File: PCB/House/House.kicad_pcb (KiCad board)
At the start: 2 copper layers, 60 x 35.5 mm, 21 parts, among them J1 Conn_01x05, U1 HT16K33-28SOP

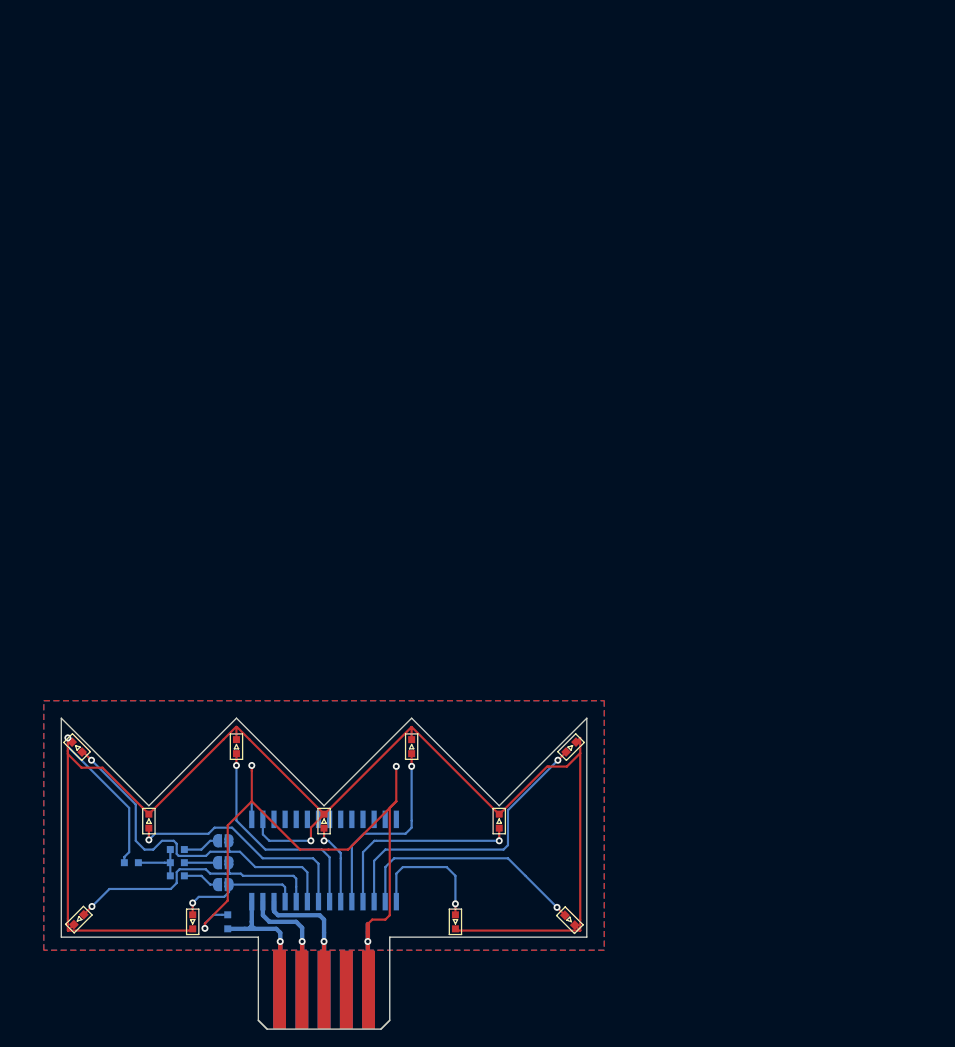
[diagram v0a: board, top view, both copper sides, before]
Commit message: [update] HouseのLED仮位置決め完了
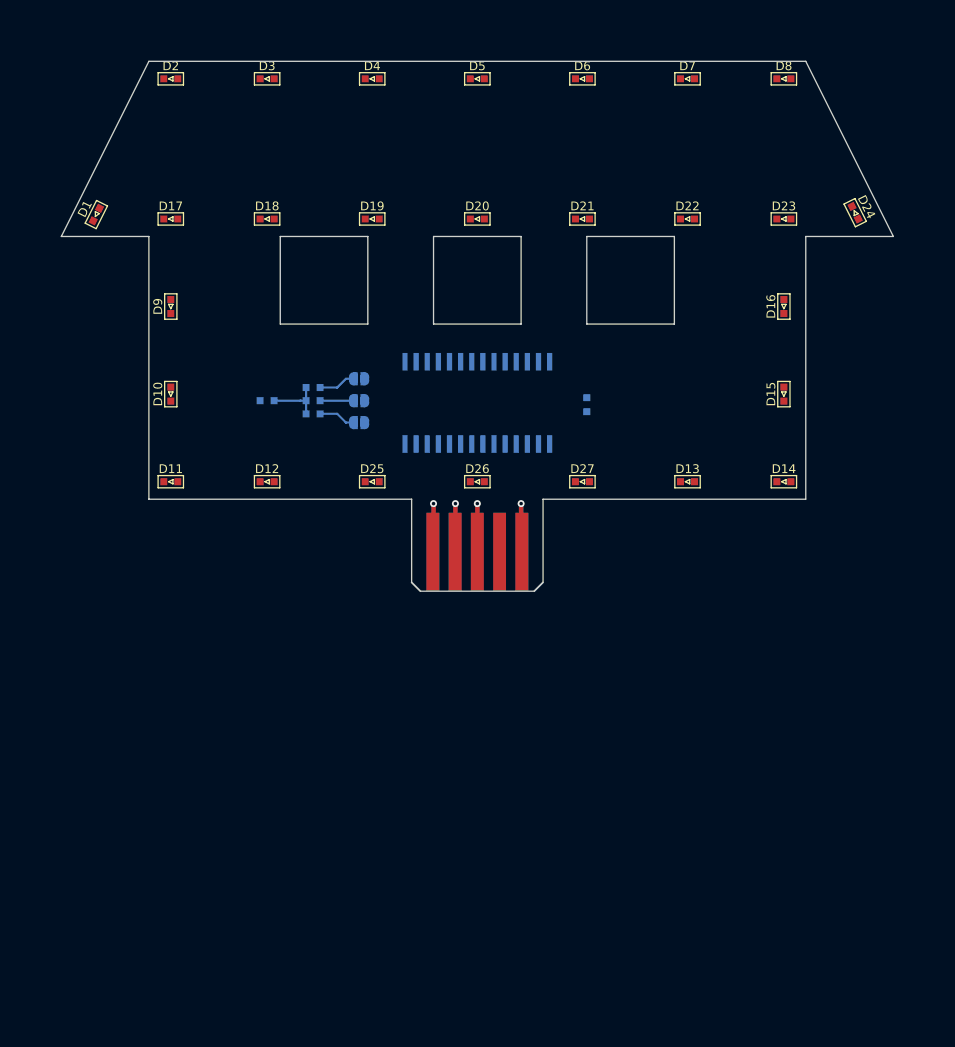
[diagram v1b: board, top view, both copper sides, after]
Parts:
- added D13: LED, extsui:LED_1608_HandSolderingCustom, F.Cu at (171.5, 98.0)
- added D14: LED, extsui:LED_1608_HandSolderingCustom, F.Cu at (182.5, 98.0)
- added D15: LED, extsui:LED_1608_HandSolderingCustom, F.Cu at (182.5, 88.0)
- added D16: LED, extsui:LED_1608_HandSolderingCustom, F.Cu at (182.5, 78.0)
- added D17: LED, extsui:LED_1608_HandSolderingCustom, F.Cu at (112.5, 68.0)
- added D18: LED, extsui:LED_1608_HandSolderingCustom, F.Cu at (123.5, 68.0)
- added D19: LED, extsui:LED_1608_HandSolderingCustom, F.Cu at (135.5, 68.0)
- added D20: LED, extsui:LED_1608_HandSolderingCustom, F.Cu at (147.5, 68.0)
- added D21: LED, extsui:LED_1608_HandSolderingCustom, F.Cu at (159.5, 68.0)
- added D22: LED, extsui:LED_1608_HandSolderingCustom, F.Cu at (171.5, 68.0)
- added D23: LED, extsui:LED_1608_HandSolderingCustom, F.Cu at (182.5, 68.0)
- added D24: LED, extsui:LED_1608_HandSolderingCustom, F.Cu at (190.6, 67.3)
- added D25: LED, extsui:LED_1608_HandSolderingCustom, F.Cu at (135.5, 98.0)
- added D26: LED, extsui:LED_1608_HandSolderingCustom, F.Cu at (147.5, 98.0)
- added D27: LED, extsui:LED_1608_HandSolderingCustom, F.Cu at (159.5, 98.0)
- added D28: D, extsui:LED_1608_HandSolderingCustom, B.Cu at (123.5, 88.8)
- D1, D10, D11, D2, D3, D4, D5, D6, D7, D8, D9: value GLED -> LED
- D12: value D -> LED; moved to F.Cu
- moved D2 96.6 mm to (112.5, 52.0), turned to 0 degrees
- moved D8 90.8 mm to (182.5, 52.0), turned to 0 degrees
- moved D6 89.7 mm to (159.5, 52.0), turned to 0 degrees
- moved D4 88.5 mm to (135.5, 52.0), turned to 0 degrees
- moved D7 82.5 mm to (171.5, 52.0), turned to 0 degrees
- moved D1 81.5 mm to (104.0, 67.5), turned to 63.4 degrees
- moved D5 81.1 mm to (147.5, 52.0), turned to 0 degrees
- moved D3 79.3 mm to (123.5, 52.0), turned to 0 degrees
- moved D10 75.4 mm to (112.5, 88.0), turned to 90 degrees
- moved C1 71.9 mm to (160.0, 89.2), turned to 270 degrees
- moved D9 68.0 mm to (112.5, 78.0), turned to 90 degrees
- moved D11 59.8 mm to (112.5, 98.0), turned to 0 degrees
- moved U1 55.1 mm to (147.5, 89.0)
- moved JP1 55.0 mm to (134.0, 91.2)
- moved JP2 55.0 mm to (134.0, 88.8)
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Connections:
- D12 pad 1: Net-(D12-Pad1) -> Net-(D1-Pad1)
- D12 pad 2: Net-(D1-Pad1) -> Net-(D12-Pad2)
- R1 pad 2: Net-(D12-Pad1) -> Net-(D28-Pad1)
- R2 pad 2: Net-(D12-Pad1) -> Net-(D28-Pad1)
- R3 pad 2: Net-(D12-Pad1) -> Net-(D28-Pad1)
- U1 pad 14: Net-(U1-Pad14) -> Net-(D12-Pad2)
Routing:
- net Net-(D1-Pad1): track 188.7 -> 0.00 mm, vias 2 -> 0
- net GND: track 82.9 -> 11.1 mm, vias 4 -> 1
- net Net-(D19-Pad2): track 40.3 -> 0.00 mm, vias 1 -> 0
- net Net-(D25-Pad2): track 34.1 -> 0.00 mm, vias 1 -> 0
- net Net-(D18-Pad2): track 31.5 -> 0.00 mm, vias 1 -> 0
- net Net-(D10-Pad2): track 27.6 -> 0.00 mm, vias 1 -> 0
- net Net-(D20-Pad2): track 27.3 -> 0.00 mm, vias 1 -> 0
- net Net-(D21-Pad2): track 25.1 -> 0.00 mm, vias 1 -> 0
- net Net-(D24-Pad2): track 23.2 -> 0.00 mm, vias 1 -> 0
- net Net-(D23-Pad2): track 22.5 -> 0.00 mm, vias 1 -> 0
- net Net-(D11-Pad2): track 15.1 -> 0.00 mm, vias 1 -> 0
- net Net-(D1-Pad2): track 15.0 -> 0.00 mm, vias 1 -> 0
- net +5V: track 21.9 -> 11.1 mm
- net SCL: track 20.7 -> 11.0 mm
- net Net-(D22-Pad2): track 9.48 -> 0.00 mm, vias 1 -> 0
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- removed copper zone on B.Cu, net GND
- removed copper zone on F.Cu, net GND
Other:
- board size 60 x 35.5 mm -> 95 x 60.5 mm
- board text added: "@ext_sui 2020.01"
- board text added: "House Growing v1.0"
- board text removed: "@ext_sui 2019.11"
- board text removed: "Grass Growing v2.1"

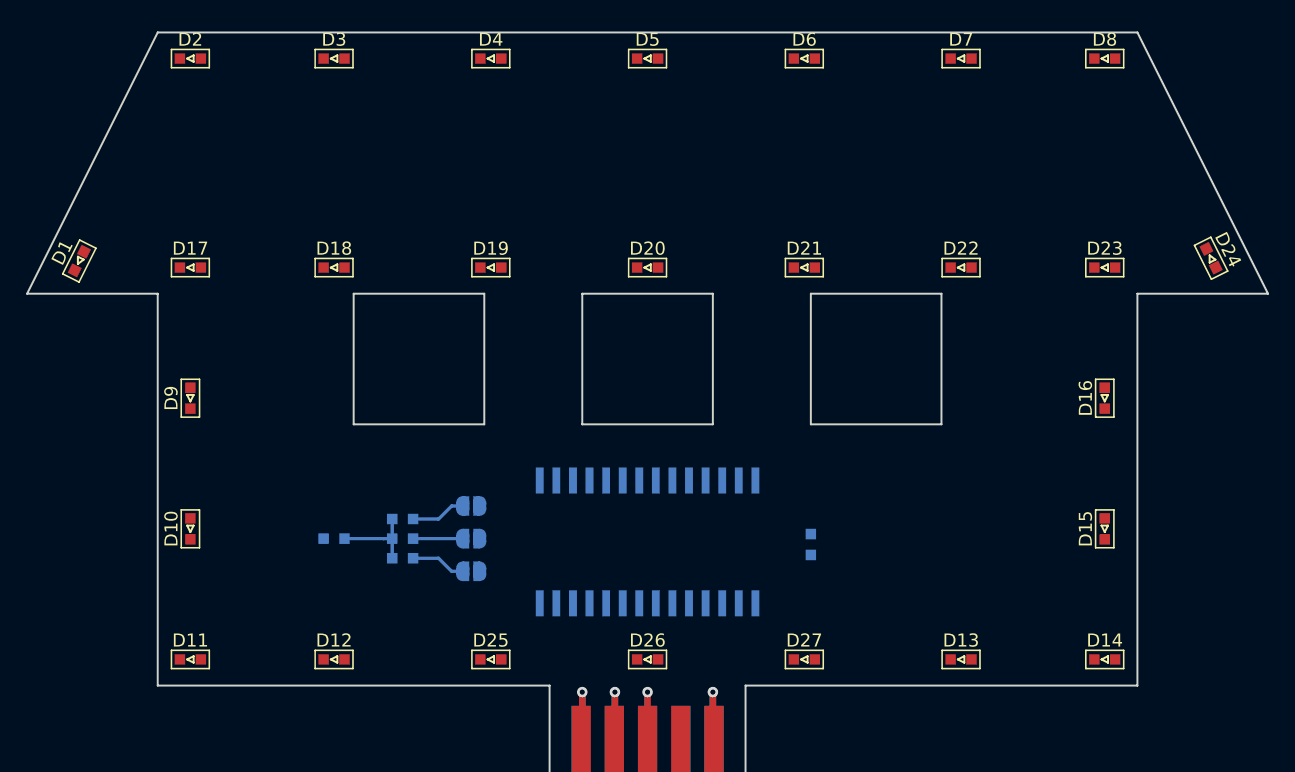
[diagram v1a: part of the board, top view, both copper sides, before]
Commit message: [update] HouseのLEDシルク裏返しと仮配線
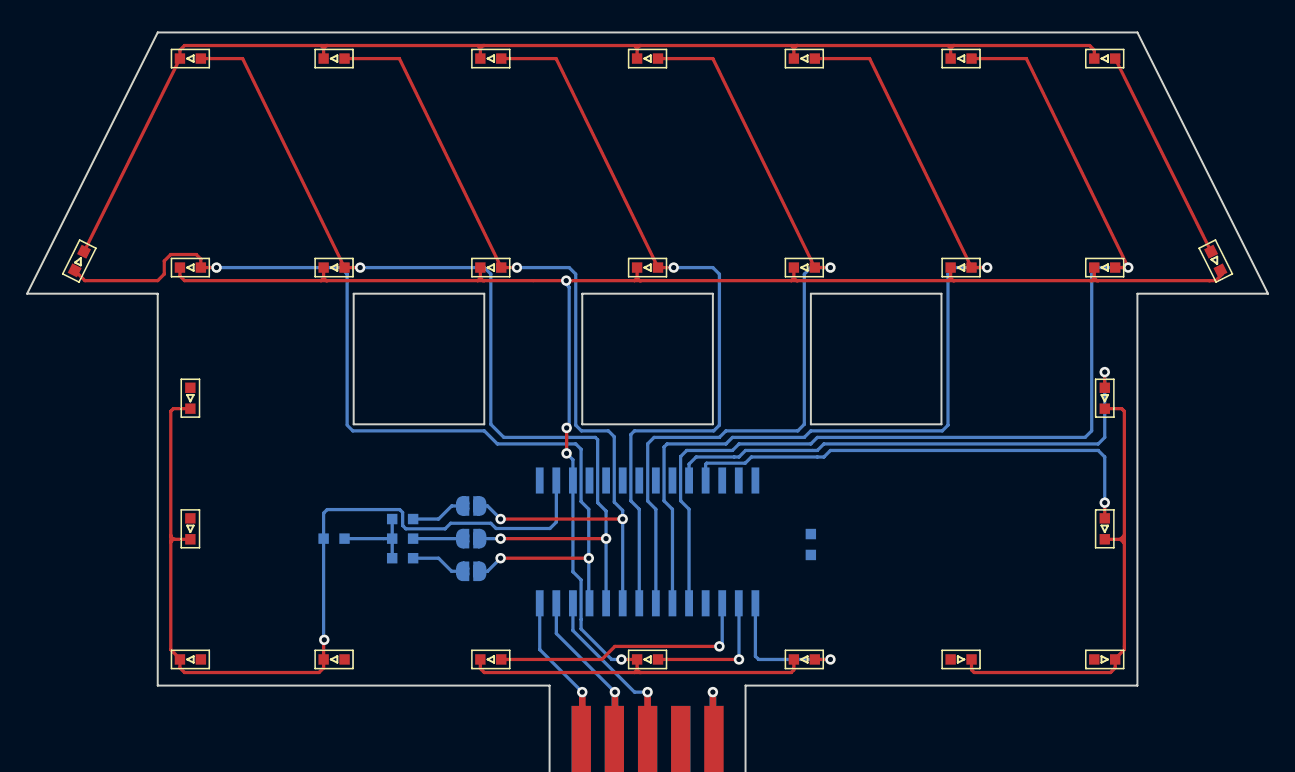
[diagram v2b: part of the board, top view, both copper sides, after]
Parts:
- moved D24 0.42 mm to (191.0, 67.5), turned to 116.6 degrees
- turned D1 to 243.4 degrees
- turned D13 to 180 degrees
- turned D14 to 180 degrees
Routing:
- net Net-(D1-Pad1): track 0.00 -> 200.6 mm, vias 0 -> 1
- net Net-(D17-Pad1): track 0.00 -> 150.0 mm, vias 0 -> 4
- net Net-(D23-Pad2): track 0.00 -> 81.8 mm, vias 0 -> 1
- net Net-(D18-Pad2): track 0.00 -> 75.0 mm, vias 0 -> 3
- net Net-(D1-Pad2): track 0.00 -> 74.6 mm, vias 0 -> 3
- net Net-(D22-Pad2): track 0.00 -> 72.6 mm, vias 0 -> 1
- net Net-(D19-Pad2): track 0.00 -> 67.2 mm, vias 0 -> 3
- net Net-(D21-Pad2): track 0.00 -> 62.0 mm, vias 0 -> 1
- net Net-(D20-Pad2): track 0.00 -> 58.7 mm, vias 0 -> 1
- net Net-(D16-Pad2): track 0.00 -> 40.1 mm, vias 0 -> 1
- net Net-(D15-Pad2): track 0.00 -> 37.1 mm, vias 0 -> 1
- net Net-(D25-Pad2): track 0.00 -> 20.5 mm, vias 0 -> 1
- net Net-(D24-Pad2): track 0.00 -> 16.5 mm
- net Net-(D11-Pad2): track 0.00 -> 11.1 mm, vias 0 -> 1
- net Net-(D10-Pad2): track 0.00 -> 10.5 mm, vias 0 -> 1
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
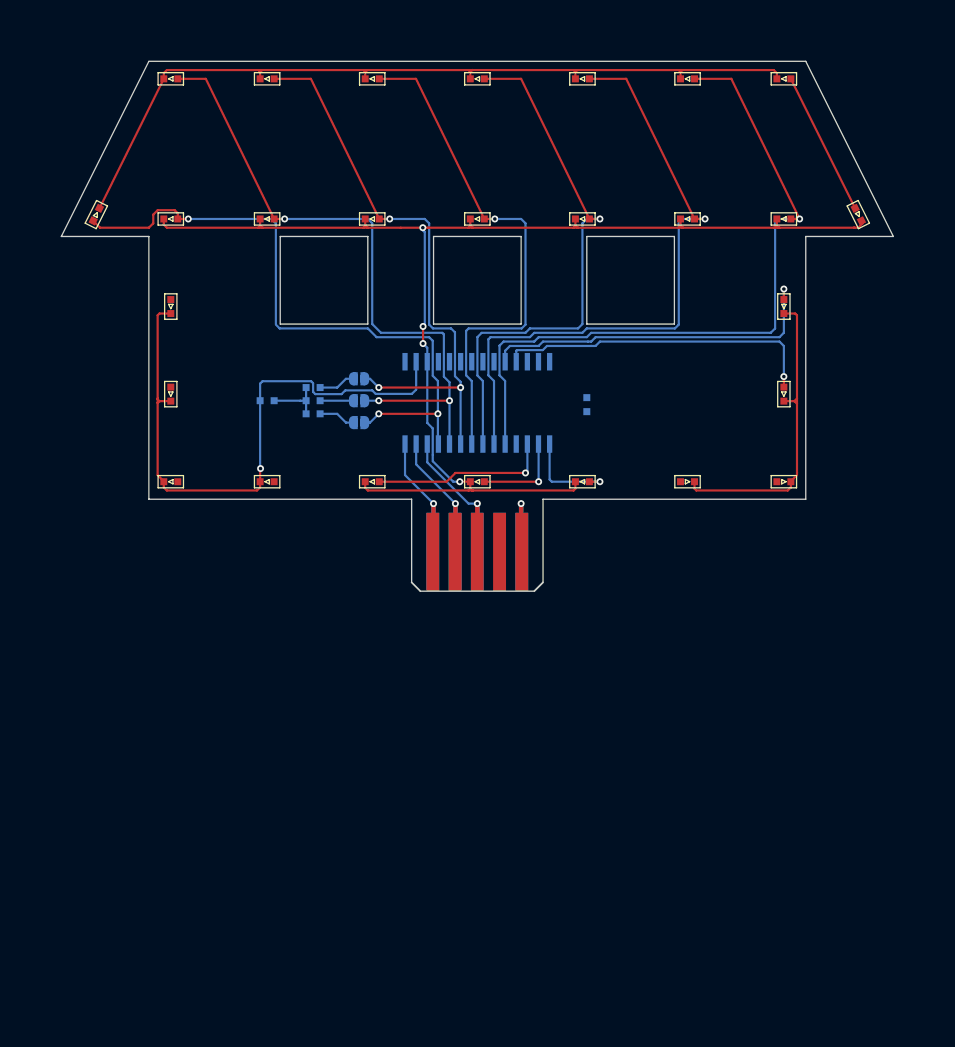
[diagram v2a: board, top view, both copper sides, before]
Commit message: [update] Houseの配線完了(初版)
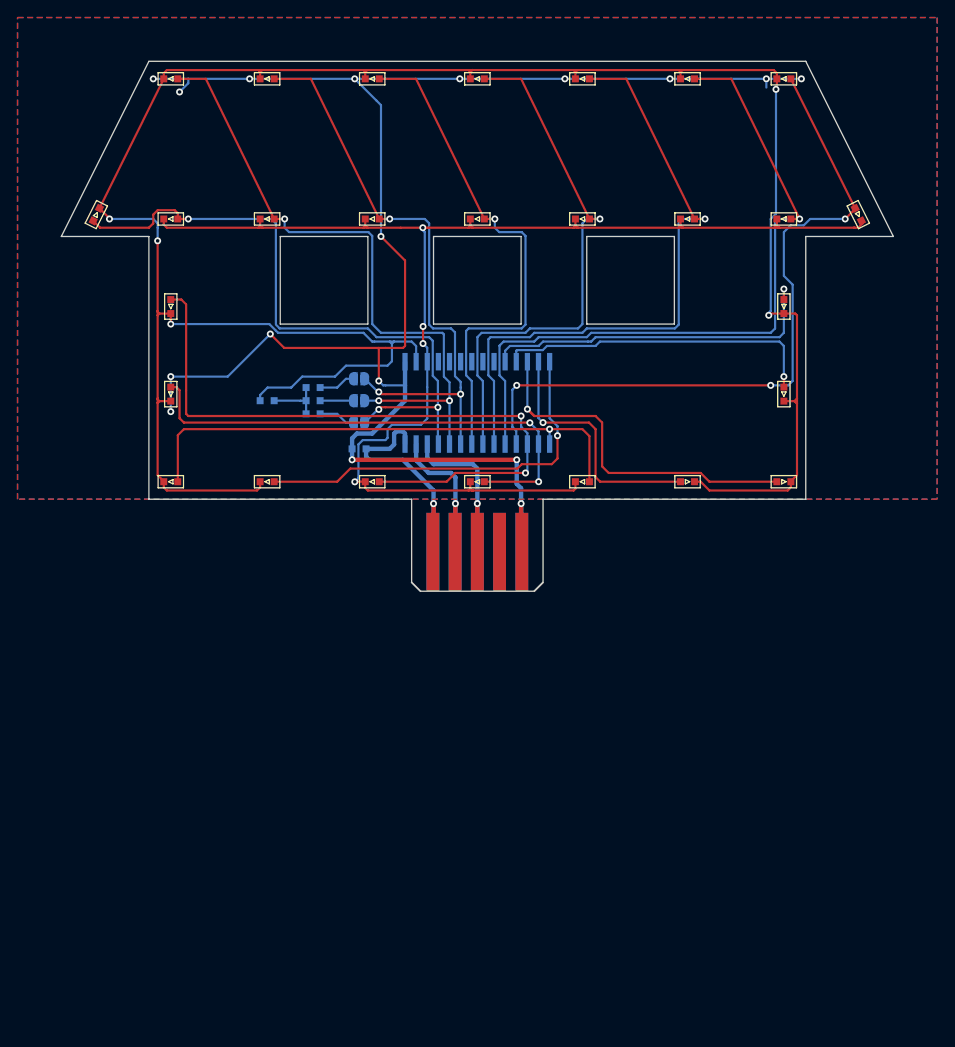
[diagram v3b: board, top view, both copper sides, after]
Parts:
- moved C1 26.5 mm to (134.0, 94.2), turned to 180 degrees
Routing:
- net GND: track 11.1 -> 200.1 mm, vias 1 -> 17
- net Net-(D24-Pad2): track 16.5 -> 82.0 mm, vias 0 -> 3
- net Net-(D1-Pad1): track 200.6 -> 265.5 mm, vias 1 -> 5
- net Net-(D25-Pad2): track 20.5 -> 76.8 mm, vias 1 -> 2
- net Net-(D11-Pad2): track 11.1 -> 59.9 mm
- net Net-(D10-Pad2): track 10.5 -> 57.9 mm, vias 1 -> 2
- net Net-(D12-Pad2): track 0.00 -> 44.9 mm, vias 0 -> 1
- net Net-(D14-Pad2): track 0.00 -> 41.4 mm, vias 0 -> 1
- net Net-(D13-Pad2): track 0.00 -> 29.1 mm, vias 0 -> 1
- net +5V: track 19.2 -> 30.1 mm
- net Net-(D17-Pad1): track 150.0 -> 154.9 mm
- net SCL: track 20.8 -> 22.8 mm
- net SDA: track 19.7 -> 21.2 mm
- added copper zone on B.Cu, net GND
- added copper zone on F.Cu, net GND
